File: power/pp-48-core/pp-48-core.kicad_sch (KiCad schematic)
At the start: 0 parts

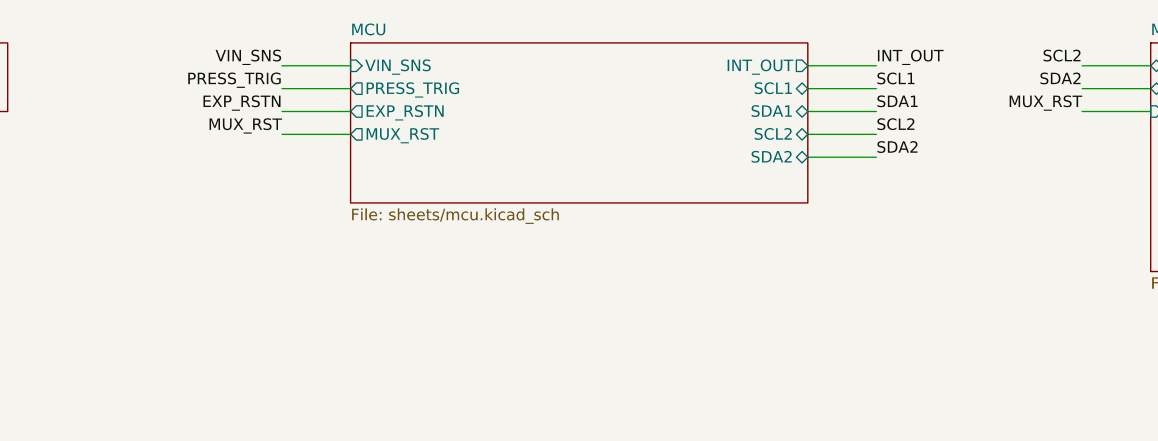
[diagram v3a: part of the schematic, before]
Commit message: pp-48 core MCU: pins reassigned for the fewest ratsnest crossings on the core board (38 -> 13): I2C1 PB8 / PB9, I2C2 PA11 / PA12, VIN_SNS PB11, PRESS_TRIG PB12, MUX_RST PB13, LED_RUN PB14, EXP_RSTN PD0, INT_OUT PD2, ADR0-2 PA15 / PD1 / PA8; MCU sheet drawn from the pin map (ports / labels at the pins); gensch.py core writes firmware/plane-core-pins.toml from the same table; ADR 0002 pin table, ADR 0005 and the press-deadline note follow; ERC 0
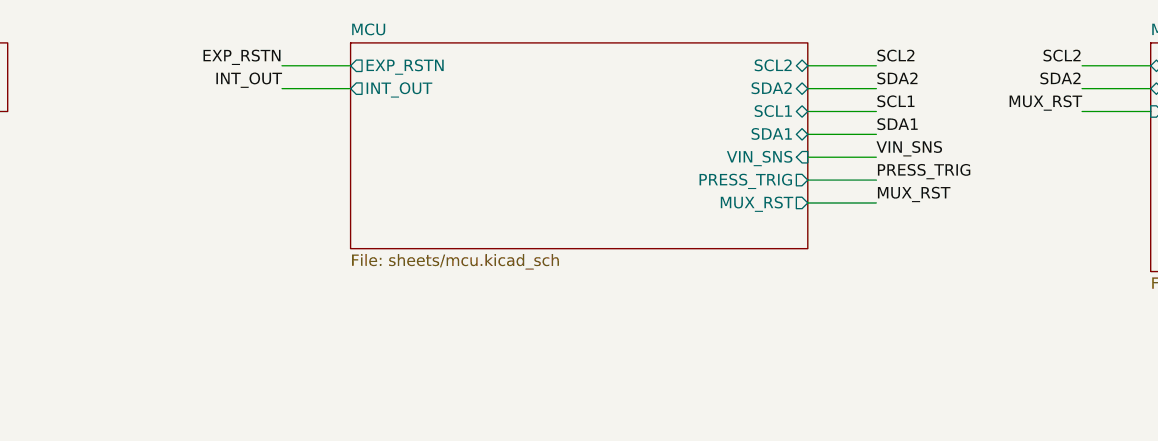
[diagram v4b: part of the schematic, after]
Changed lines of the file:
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@@
 	(sheet
 		(at 215.9 38.1)
-		(size 50.8 17.78)
+		(size 50.8 22.86)
 		(exclude_from_sim no)
 		(in_bom yes)
@@
 		)
 		(property "Sheetfile" "sheets/mcu.kicad_sch"
-			(at 215.9 56.4684 0)
+			(at 215.9 61.5484 0)
 			(show_name no)
 			(do_not_autoplace no)
@@
 			)
 		)
+		(pin "EXP_RSTN" output
+			(at 215.9 40.64 180)
+			(effects
+				(font
+					(size 1.27 1.27)
+				)
+				(justify left)
+			)
+		)
+		(pin "INT_OUT" output
+			(at 215.9 43.18 180)
+			(effects
+				(font
+					(size 1.27 1.27)
+				)
+				(justify left)
+			)
+		)
+		(pin "SCL2" bidirectional
+			(at 266.7 40.64 0)
+			(effects
+				(font
+					(size 1.27 1.27)
+				)
+				(justify right)
+			)
+		)
+		(pin "SDA2" bidirectional
+			(at 266.7 43.18 0)
+			(effects
+				(font
+					(size 1.27 1.27)
+				)
+				(justify right)
+			)
+		)
+		(pin "SCL1" bidirectional
+			(at 266.7 45.72 0)
+			(effects
+				(font
+					(size 1.27 1.27)
+				)
+				(justify right)
+			)
+		)
+		(pin "SDA1" bidirectional
+			(at 266.7 48.26 0)
+			(effects
+				(font
+					(size 1.27 1.27)
+				)
+				(justify right)
+			)
+		)
 		(pin "VIN_SNS" input
-			(at 215.9 40.64 180)
-			(effects
-				(font
-					(size 1.27 1.27)
-				)
-				(justify left)
+			(at 266.7 50.8 0)
+			(effects
+				(font
+					(size 1.27 1.27)
+				)
+				(justify right)
 			)
 		)
 		(pin "PRESS_TRIG" output
-			(at 215.9 43.18 180)
-			(effects
-				(font
-					(size 1.27 1.27)
-				)
-				(justify left)
-			)
-		)
-		(pin "EXP_RSTN" output
-			(at 215.9 45.72 180)
-			(effects
-				(font
-					(size 1.27 1.27)
-				)
-				(justify left)
+			(at 266.7 53.34 0)
+			(effects
+				(font
+					(size 1.27 1.27)
+				)
+				(justify right)
 			)
 		)
 		(pin "MUX_RST" output
-			(at 215.9 48.26 180)
-			(effects
-				(font
-					(size 1.27 1.27)
-				)
-				(justify left)
-			)
-		)
-		(pin "INT_OUT" output
-			(at 266.7 40.64 0)
-			(effects
-				(font
-					(size 1.27 1.27)
-				)
-				(justify right)
-			)
-		)
-		(pin "SCL1" bidirectional
-			(at 266.7 43.18 0)
-			(effects
-				(font
-					(size 1.27 1.27)
-				)
-				(justify right)
-			)
-		)
-		(pin "SDA1" bidirectional
-			(at 266.7 45.72 0)
-			(effects
-				(font
-					(size 1.27 1.27)
-				)
-				(justify right)
-			)
-		)
-		(pin "SCL2" bidirectional
-			(at 266.7 48.26 0)
-			(effects
-				(font
-					(size 1.27 1.27)
-				)
-				(justify right)
-			)
-		)
-		(pin "SDA2" bidirectional
-			(at 266.7 50.8 0)
+			(at 266.7 55.88 0)
 			(effects
 				(font
@@
 		)
 	)
+	(label "EXP_RSTN"
+		(at 208.28 40.64 180)
+		(effects
+			(font
+				(size 1.27 1.27)
+			)
+			(justify right bottom)
+		)
+	)
+	(wire
+		(pts
+			(xy 215.9 43.18) (xy 208.28 43.18)
+		)
+		(stroke
+			(width 0)
+			(type default)
+		)
+	)
+	(label "INT_OUT"
+		(at 208.28 43.18 180)
+		(effects
+			(font
+				(size 1.27 1.27)
+			)
+			(justify right bottom)
+		)
+	)
+	(wire
+		(pts
+			(xy 266.7 40.64) (xy 274.32 40.64)
+		)
+		(stroke
+			(width 0)
+			(type default)
+		)
+	)
+	(label "SCL2"
+		(at 274.32 40.64 0)
+		(effects
+			(font
+				(size 1.27 1.27)
+			)
+			(justify left bottom)
+		)
+	)
+	(wire
+		(pts
+			(xy 266.7 43.18) (xy 274.32 43.18)
+		)
+		(stroke
+			(width 0)
+			(type default)
+		)
+	)
+	(label "SDA2"
+		(at 274.32 43.18 0)
+		(effects
+			(font
+				(size 1.27 1.27)
+			)
+			(justify left bottom)
+		)
+	)
+	(wire
+		(pts
+			(xy 266.7 45.72) (xy 274.32 45.72)
+		)
+		(stroke
+			(width 0)
+			(type default)
+		)
+	)
+	(label "SCL1"
+		(at 274.32 45.72 0)
+		(effects
+			(font
+				(size 1.27 1.27)
+			)
+			(justify left bottom)
+		)
+	)
+	(wire
+		(pts
+			(xy 266.7 48.26) (xy 274.32 48.26)
+		)
+		(stroke
+			(width 0)
+			(type default)
+		)
+	)
+	(label "SDA1"
+		(at 274.32 48.26 0)
+		(effects
+			(font
+				(size 1.27 1.27)
+			)
+			(justify left bottom)
+		)
+	)
+	(wire
+		(pts
+			(xy 266.7 50.8) (xy 274.32 50.8)
+		)
+		(stroke
+			(width 0)
+			(type default)
+		)
+	)
 	(label "VIN_SNS"
-		(at 208.28 40.64 180)
-		(effects
-			(font
-				(size 1.27 1.27)
-			)
-			(justify right bottom)
-		)
-	)
-	(wire
-		(pts
-			(xy 215.9 43.18) (xy 208.28 43.18)
+		(at 274.32 50.8 0)
+		(effects
+			(font
+				(size 1.27 1.27)
+			)
+			(justify left bottom)
+		)
+	)
+	(wire
+		(pts
+			(xy 266.7 53.34) (xy 274.32 53.34)
 		)
 		(stroke
@@
 	)
 	(label "PRESS_TRIG"
-		(at 208.28 43.18 180)
-		(effects
-			(font
-				(size 1.27 1.27)
-			)
-			(justify right bottom)
-		)
-	)
-	(wire
-		(pts
-			(xy 215.9 45.72) (xy 208.28 45.72)
-		)
-		(stroke
-			(width 0)
-			(type default)
-		)
-	)
-	(label "EXP_RSTN"
-		(at 208.28 45.72 180)
-		(effects
-			(font
-				(size 1.27 1.27)
-			)
-			(justify right bottom)
-		)
-	)
-	(wire
-		(pts
-			(xy 215.9 48.26) (xy 208.28 48.26)
+		(at 274.32 53.34 0)
+		(effects
+			(font
+				(size 1.27 1.27)
+			)
+			(justify left bottom)
+		)
+	)
+	(wire
+		(pts
+			(xy 266.7 55.88) (xy 274.32 55.88)
 		)
 		(stroke
@@
 	)
 	(label "MUX_RST"
-		(at 208.28 48.26 180)
-		(effects
-			(font
-				(size 1.27 1.27)
-			)
-			(justify right bottom)
-		)
-	)
-	(wire
-		(pts
-			(xy 266.7 40.64) (xy 274.32 40.64)
-		)
-		(stroke
-			(width 0)
-			(type default)
-		)
-	)
-	(label "INT_OUT"
-		(at 274.32 40.64 0)
-		(effects
-			(font
-				(size 1.27 1.27)
-			)
-			(justify left bottom)
-		)
-	)
-	(wire
-		(pts
-			(xy 266.7 43.18) (xy 274.32 43.18)
-		)
-		(stroke
-			(width 0)
-			(type default)
-		)
-	)
-	(label "SCL1"
-		(at 274.32 43.18 0)
-		(effects
-			(font
-				(size 1.27 1.27)
-			)
-			(justify left bottom)
-		)
-	)
-	(wire
-		(pts
-			(xy 266.7 45.72) (xy 274.32 45.72)
-		)
-		(stroke
-			(width 0)
-			(type default)
-		)
-	)
-	(label "SDA1"
-		(at 274.32 45.72 0)
-		(effects
-			(font
-				(size 1.27 1.27)
-			)
-			(justify left bottom)
-		)
-	)
-	(wire
-		(pts
-			(xy 266.7 48.26) (xy 274.32 48.26)
-		)
-		(stroke
-			(width 0)
-			(type default)
-		)
-	)
-	(label "SCL2"
-		(at 274.32 48.26 0)
-		(effects
-			(font
-				(size 1.27 1.27)
-			)
-			(justify left bottom)
-		)
-	)
-	(wire
-		(pts
-			(xy 266.7 50.8) (xy 274.32 50.8)
-		)
-		(stroke
-			(width 0)
-			(type default)
-		)
-	)
-	(label "SDA2"
-		(at 274.32 50.8 0)
-		(effects
-			(font
+		(at 274.32 55.88 0)
+		(effects
+			(font
